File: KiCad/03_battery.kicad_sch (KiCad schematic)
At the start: 19 parts, among them IC301 MCP73831T-2ACI_OT, IC302 BQ29737DSER, J302 BM02B-GHS-TBT_LF__SN__N_, Q201 DMG3415U-7, Q202 T2N7002AK, Q500 T2N7002AK

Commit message: First scheme complete
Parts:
- renumbered C211 to C301, C212 to C302, C215 to C303, C214 to C304, C213 to C305, D202 to D301, D205 to D302, FB203 to FB301, J302 to J301, Q201 to Q301, Q202 to Q302, Q500 to Q303, R201 to R301, R206 to R302, R209 to R303, R210 to R304, R211 to R305

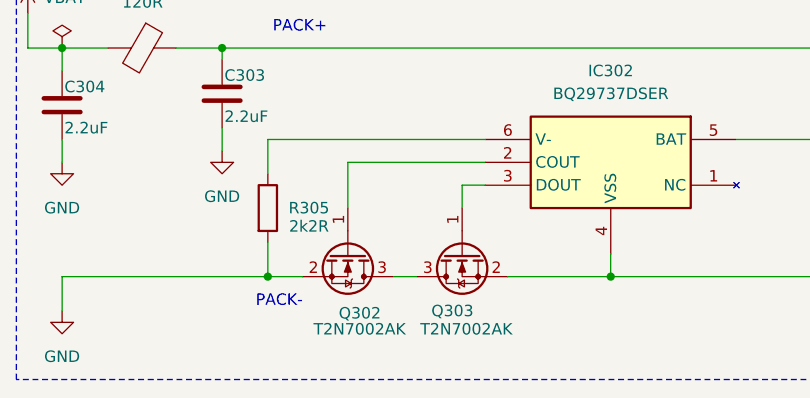
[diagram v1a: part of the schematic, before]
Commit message: ERC fixes
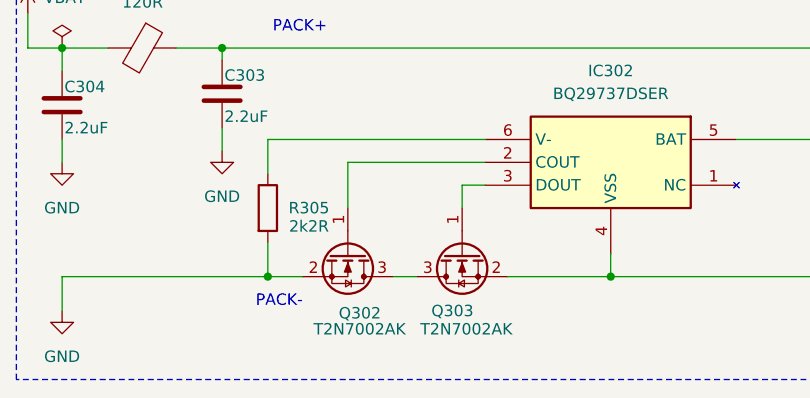
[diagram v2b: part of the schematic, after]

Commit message: minor pcb update
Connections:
- net COUT: now reaches IC302.2 (COUT), Q302.1 (G)
- net DOUT: now reaches IC302.3 (DOUT), Q303.1 (G)
- net V-: now reaches IC302.6 (V-), R305.1
- net BAT: now reaches C305.1, IC302.5 (BAT), R304.2

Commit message: Update FTDI pin header
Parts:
- R304: footprint Resistor_SMD:R_0805_2012Metric -> Resistor_SMD:R_0402_1005Metric
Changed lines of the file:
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@@
 			)
 		)
-		(property "Footprint" "Resistor_SMD:R_0805_2012Metric"
+		(property "Footprint" "Resistor_SMD:R_0402_1005Metric"
 			(at 135.382 143.51 90)
 			(effects

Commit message: Fill BOM table
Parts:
- IC301: Manufacturer (none) -> Microchip; Manufacturer Part Number (none) -> MCP73831T-2ACI/OT; Manufacturer_Name Microchip -> (none); Manufacturer_Part_Number MCP73831T-2ACI/OT -> (none); Mouser Part Number 579-MCP73831T-2ACIOT -> (none); Mouser Price/Stock https://www.mouser.co.uk/ProductDetail/Microchip-Technology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 -> (none)
- IC302: Manufacturer (none) -> Texas Instruments; Manufacturer Part Number (none) -> BQ29737DSER; Manufacturer_Name Texas Instruments -> (none); Manufacturer_Part_Number BQ29737DSER -> (none); Mouser Part Number 595-BQ29737DSER -> (none); Mouser Price/Stock https://www.mouser.co.uk/ProductDetail/Texas-Instruments/BQ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 -> (none)
- J301: Manufacturer (none) -> JST (JAPAN SOLDERLESS TERMINALS); Manufacturer Part Number (none) -> BM02B-GHS-TBT(LF)(SN)(N); Manufacturer_Name JST (JAPAN SOLDERLESS TERMINALS) -> (none); Manufacturer_Part_Number BM02B-GHS-TBT(LF)(SN)(N) -> (none)
- R303: LCSC link https://www.lcsc.com/product-detail/Chip-Resistor-Surface-M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 -> (none)
- R304: Manufacturer (none) -> UNI-ROYAL(Uniroyal Elec); Manufacturer Part Number (none) -> 0402WGF3300TCE
- R305: footprint Resistor_SMD:R_0805_2012Metric -> Resistor_SMD:R_0402_1005Metric; Manufacturer (none) -> UNI-ROYAL(Uniroyal Elec); Manufacturer Part Number (none) -> 0402WGF2201TCE
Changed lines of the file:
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@@
-			)
-		)
-		(property "Manufacturer_Name" "JST (JAPAN SOLDERLESS TERMINALS)"
-			(at 648.59 146.05 0)
-			(effects
-				(font
-					(size 1.27 1.27)
-				)
-				(justify left top)
-				(hide yes)
-			)
-		)
-		(property "Manufacturer_Part_Number" "BM02B-GHS-TBT(LF)(SN)(N)"
-			(at 748.59 146.05 0)
-			(effects
-				(font
-					(size 1.27 1.27)
-				)
-				(justify left top)
-				(hide yes)
-			)
-		)
-		(property "Mouser Part Number" ""
-			(at 848.59 146.05 0)
-			(effects
-				(font
-					(size 1.27 1.27)
-				)
-				(justify left top)
-				(hide yes)
-			)
-		)
-		(property "Mouser Price/Stock" ""
-			(at 948.59 146.05 0)
-			(effects
-				(font
-					(size 1.27 1.27)
-				)
-				(justify left top)
-				(hide yes)
 			)
 		)
@@
 				)
 				(justify left top)
+				(hide yes)
+			)
+		)
+		(property "Manufacturer" "JST (JAPAN SOLDERLESS TERMINALS)"
+			(at 153.67 162.56 90)
+			(effects
+				(font
+					(size 1.27 1.27)
+				)
+				(hide yes)
+			)
+		)
+		(property "Manufacturer Part Number" "BM02B-GHS-TBT(LF)(SN)(N)"
+			(at 153.67 162.56 90)
+			(effects
+				(font
+					(size 1.27 1.27)
+				)
 				(hide yes)
 			)
@@
 			)
 		)
-		(property "LCSC link" "https://www.lcsc.com/product-detail/Chip-Resistor-Surface-Mount_UNI-ROYAL-Uniroyal-Elec-0402WGF5101TCE_C25905.html"
-			(at 143.51 104.14 0)
-			(effects
-				(font
-					(size 1.27 1.27)
-				)
-				(hide yes)
-			)
-		)
 		(property "Manufacturer" "UNI-ROYAL(Uniroyal Elec)"
 			(at 143.51 104.14 0)
@@
 			)
 		)
-		(property "MANUFACTURER" ""
-			(at 100.33 87.63 0)
-			(effects
-				(font
-					(size 1.27 1.27)
-				)
-				(hide yes)
-			)
-		)
 		(property "PARTREV" ""
 			(at 100.33 87.63 0)
@@
 			)
 		)
-		(property "MANUFACTURER" ""
-			(at 48.26 144.78 0)
-			(effects
-				(font
-					(size 1.27 1.27)
-				)
-				(hide yes)
-			)
-		)
 		(property "PARTREV" ""
 			(at 48.26 144.78 0)
@@
 			)
 		)
-		(property "MANUFACTURER" ""
-			(at 66.04 143.51 0)
-			(effects
-				(font
-					(size 1.27 1.27)
-				)
-				(hide yes)
-			)
-		)
 		(property "PARTREV" ""
 			(at 66.04 143.51 0)
@@
 			)
 		)
-		(property "Footprint" "Resistor_SMD:R_0805_2012Metric"
+		(property "Footprint" "Resistor_SMD:R_0402_1005Metric"
 			(at 69.342 156.21 90)
 			(effects
@@
 			)
 		)
-		(property "Manufacturer" ""
+		(property "Manufacturer" "UNI-ROYAL(Uniroyal Elec)"
 			(at 71.12 156.21 0)
 			(effects
@@
 			)
 		)
-		(property "Manufacturer Part Number" ""
-			(at 71.12 156.21 0)
-			(effects
-				(font
-					(size 1.27 1.27)
-				)
-				(hide yes)
-			)
-		)
-		(property "MANUFACTURER" ""
+		(property "Manufacturer Part Number" "0402WGF2201TCE"
 			(at 71.12 156.21 0)
 			(effects
@@
 			)
 		)
-		(property "Manufacturer_Name" "Microchip"
-			(at 134.62 591.44 0)
-			(effects
-				(font
-					(size 1.27 1.27)
-				)
-				(justify left top)
-				(hide yes)
-			)
-		)
-		(property "Manufacturer_Part_Number" "MCP73831T-2ACI/OT"
-			(at 134.62 691.44 0)
-			(effects
-				(font
-					(size 1.27 1.27)
-				)
-				(justify left top)
-				(hide yes)
-			)
-		)
-		(property "Mouser Part Number" "579-MCP73831T-2ACIOT"
-			(at 134.62 791.44 0)
-			(effects
-				(font
-					(size 1.27 1.27)
-				)
-				(justify left top)
-				(hide yes)
-			)
-		)
-		(property "Mouser Price/Stock" "https://www.mouser.co.uk/ProductDetail/Microchip-Technology/MCP73831T-2ACI-OT?qs=yUQqVecv4qvbBQBGbHx0Mw%3D%3D"
-			(at 134.62 891.44 0)
-			(effects
-				(font
-					(size 1.27 1.27)
-				)
-				(justify left top)
-				(hide yes)
-			)
-		)
 		(property "Arrow Part Number" "MCP73831T-2ACI/OT"
 			(at 134.62 991.44 0)
@@
 				)
 				(justify left top)
+				(hide yes)
+			)
+		)
+		(property "Manufacturer" "Microchip"
+			(at 110.49 96.52 0)
+			(effects
+				(font
+					(size 1.27 1.27)
+				)
+				(hide yes)
+			)
+		)
+		(property "Manufacturer Part Number" "MCP73831T-2ACI/OT"
+			(at 110.49 96.52 0)
+			(effects
+				(font
+					(size 1.27 1.27)
+				)
 				(hide yes)
 			)
@@
 			)
 		)
-		(property "Manufacturer" ""
+		(property "Manufacturer" "UNI-ROYAL(Uniroyal Elec)"
 			(at 137.16 143.51 0)
 			(effects
@@
 			)
 		)
-		(property "Manufacturer Part Number" ""
-			(at 137.16 143.51 0)
-			(effects
-				(font
-					(size 1.27 1.27)
-				)
-				(hide yes)
-			)
-		)
-		(property "MANUFACTURER" ""
+		(property "Manufacturer Part Number" "0402WGF3300TCE"
 			(at 137.16 143.51 0)
 			(effects
@@
 			)
 		)
-		(property "MANUFACTURER" ""
-			(at 149.86 92.71 0)
-			(effects
-				(font
-					(size 1.27 1.27)
-				)
-				(hide yes)
-			)
-		)
 		(property "PARTREV" ""
 			(at 149.86 92.71 0)
@@
 			)
 		)
-		(property "Manufacturer_Name" "Texas Instruments"
-			(at 93.98 640.97 0)
-			(effects
-				(font
-					(size 1.27 1.27)
-				)
-				(justify left top)
-				(hide yes)
-			)
-		)
-		(property "Manufacturer_Part_Number" "BQ29737DSER"
-			(at 93.98 740.97 0)
-			(effects
-				(font
-					(size 1.27 1.27)
-				)
-				(justify left top)
-				(hide yes)
-			)
-		)
-		(property "Mouser Part Number" "595-BQ29737DSER"
-			(at 93.98 840.97 0)
-			(effects
-				(font
-					(size 1.27 1.27)
-				)
-				(justify left top)
-				(hide yes)
-			)
-		)
-		(property "Mouser Price/Stock" "https://www.mouser.co.uk/ProductDetail/Texas-Instruments/BQ29737DSER?qs=QNEnbhJQKvZFYvtkppP%2FHQ%3D%3D"
-			(at 93.98 940.97 0)
-			(effects
-				(font
-					(size 1.27 1.27)
-				)
-				(justify left top)
-				(hide yes)
-			)
-		)
 		(property "Arrow Part Number" "BQ29737DSER"
 			(at 93.98 1040.97 0)
@@
 				)
 				(justify left top)
+				(hide yes)
+			)
+		)
+		(property "Manufacturer" "Texas Instruments"
+			(at 118.11 146.05 0)
+			(effects
+				(font
+					(size 1.27 1.27)
+				)
+				(hide yes)
+			)
+		)
+		(property "Manufacturer Part Number" "BQ29737DSER"
+			(at 118.11 146.05 0)
+			(effects
+				(font
+					(size 1.27 1.27)
+				)
 				(hide yes)
 			)
@@
 			)
 		)
-		(property "MANUFACTURER" ""
-			(at 137.16 158.75 0)
-			(effects
-				(font
-					(size 1.27 1.27)
-				)
-				(hide yes)
-			)
-		)
 		(property "PARTREV" ""
 			(at 137.16 158.75 0)
@@
 			(at 132.08 53.34 0)
 			(effects
-				(font
-					(size 1.27 1.27)
-				)
-				(hide yes)
-			)
-		)
-		(property "MANUFACTURER" ""
-			(at 132.08 53.34 0)
-			(effects

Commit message: battery connector update
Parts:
- removed J301: BM02B-GHS-TBT_LF__SN__N_, psu:BM02B-GHS-TBT_1, symbol psu:BM02B-GHS-TBT_LF__SN__N_
- added J301: Conn_01x02, Connector_PinHeader_2.54mm:PinHeader_1x02_P2.54mm_Vertical, symbol Connector_Generic:Conn_01x02
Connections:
- net CELL+: now also J301.1 (Pin_1)
- net CELL-: now also J301.2 (Pin_2)
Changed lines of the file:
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@@
 	(wire
 		(pts
-			(xy 153.67 138.43) (xy 153.67 142.24)
+			(xy 153.67 138.43) (xy 153.67 149.86)
 		)
 		(stroke
@@
 	(wire
 		(pts
-			(xy 153.67 163.83) (xy 153.67 162.56)
+			(xy 153.67 152.4) (xy 153.67 163.83)
 		)
 		(stroke
@@
 	)
 	(symbol
-		(lib_id "psu:BM02B-GHS-TBT_LF__SN__N_")
-		(at 153.67 162.56 90)
-		(unit 1)
-		(exclude_from_sim no)
-		(in_bom yes)
-		(on_board yes)
-		(dnp no)
-		(property "Reference" "J301"
-			(at 145.288 152.4 90)
-			(effects
-				(font
-					(size 1.27 1.27)
-				)
-				(justify right)
-			)
-		)
-		(property "Value" "BM02B-GHS-TBT_LF__SN__N_"
-			(at 158.496 137.414 0)
-			(effects
-				(font
-					(size 1.27 1.27)
-				)
-				(justify right)
-			)
-		)
-		(property "Footprint" "psu:BM02B-GHS-TBT_1"
-			(at 248.59 146.05 0)
-			(effects
-				(font
-					(size 1.27 1.27)
-				)
-				(justify left top)
-				(hide yes)
-			)
-		)
-		(property "Datasheet" "http://www.jst-mfg.com/product/pdf/eng/eGH.pdf"
-			(at 348.59 146.05 0)
-			(effects
-				(font
-					(size 1.27 1.27)
-				)
-				(justify left top)
-				(hide yes)
-			)
-		)
-		(property "Description" "CONN HEADER GH TOP 2POS 1.25MM"
-			(at 159.004 149.606 0)
-			(effects
-				(font
-					(size 1.27 1.27)
-				)
-				(hide yes)
-			)
-		)
-		(property "Height" ""
-			(at 548.59 146.05 0)
-			(effects
-				(font
-					(size 1.27 1.27)
-				)
-				(justify left top)
-				(hide yes)
-			)
-		)
-		(property "Arrow Part Number" "BM02B-GHS-TBT(LF)(SN)(N)"
-			(at 1048.59 146.05 0)
-			(effects
-				(font
-					(size 1.27 1.27)
-				)
-				(justify left top)
-				(hide yes)
-			)
-		)
-		(property "Arrow Price/Stock" "https://www.arrow.com/en/products/bm02b-ghs-tbt-lf-sn-n/jst-manufacturing?region=nac"
-			(at 1148.59 146.05 0)
-			(effects
-				(font
-					(size 1.27 1.27)
-				)
-				(justify left top)
-				(hide yes)
-			)
-		)
-		(property "Manufacturer" "JST (JAPAN SOLDERLESS TERMINALS)"
-			(at 153.67 162.56 90)
-			(effects
-				(font
-					(size 1.27 1.27)
-				)
-				(hide yes)
-			)
-		)
-		(property "Manufacturer Part Number" "BM02B-GHS-TBT(LF)(SN)(N)"
-			(at 153.67 162.56 90)
-			(effects
-				(font
-					(size 1.27 1.27)
-				)
-				(hide yes)
-			)
-		)
-		(pin "2"
-		)
-		(pin "1"
-		)
-		(instances
-			(project ""
-				(path "/daadd221-9750-45f3-8ee2-46422755319d/b34b4305-fc5f-4a45-8a4d-fa6c9d60dff6"
-					(reference "J301")
-					(unit 1)
-				)
-			)
-		)
-	)
-	(symbol
 		(lib_id "Transistor_FET:T2N7002AK")
 		(at 92.71 161.29 90)
@@
 					(unit 1)
 				)
+			)
+		)
+	)
+	(symbol
+		(lib_id "Connector_Generic:Conn_01x02")
+		(at 158.75 149.86 0)
+		(unit 1)
+		(exclude_from_sim no)
+		(in_bom yes)
+		(on_board yes)
+		(dnp no)
+		(property "Reference" "J301"
+			(at 156.21 146.304 0)
+			(effects
+				(font
+					(size 1.27 1.27)
+				)
+				(justify left)
+			)
+		)
+		(property "Value" "Conn_01x02"
+			(at 153.416 155.702 0)
+			(effects
+				(font
+					(size 1.27 1.27)
+				)
+				(justify left)
+			)
+		)
+		(property "Footprint" "Connector_PinHeader_2.54mm:PinHeader_1x02_P2.54mm_Vertical"
+			(at 158.75 149.86 0)
+			(effects
+				(font
+					(size 1.27 1.27)
+				)
+				(hide yes)
+			)
+		)
+		(property "Datasheet" "~"
+			(at 158.75 149.86 0)
+			(effects
+				(font
+					(size 1.27 1.27)
+				)
+				(hide yes)
+			)
+		)
+		(property "Description" "Generic connector, single row, 01x02, script generated (kicad-library-utils/schlib/autogen/connector/)"
+			(at 158.75 149.86 0)
+			(effects
+				(font
+					(size 1.27 1.27)
+				)
+				(hide yes)
+			)
+		)
+		(pin "1"
+		)
+		(pin "2"
+		)
+		(instances
+			(project ""
+				(path "/daadd221-9750-45f3-8ee2-46422755319d/b34b4305-fc5f-4a45-8a4d-fa6c9d60dff6"
+					(reference "J301")
+					(unit 1)
+				)

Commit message: BOM updates
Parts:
- R301, R302, R303, R304, R305: Manufacturer UNI-ROYAL(Uniroyal Elec) -> UNI-ROYAL
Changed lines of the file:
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@@
 			)
 		)
-		(property "Manufacturer" "UNI-ROYAL(Uniroyal Elec)"
+		(property "Manufacturer" "UNI-ROYAL"
 			(at 88.9 91.44 0)
 			(effects
@@
 			)
 		)
-		(property "Manufacturer" "UNI-ROYAL(Uniroyal Elec)"
+		(property "Manufacturer" "UNI-ROYAL"
 			(at 143.51 104.14 0)
 			(effects
@@
 			)
 		)
-		(property "Manufacturer" "UNI-ROYAL(Uniroyal Elec)"
+		(property "Manufacturer" "UNI-ROYAL"
 			(at 71.12 156.21 0)
 			(effects
@@
 			)
 		)
-		(property "Manufacturer" "UNI-ROYAL(Uniroyal Elec)"
+		(property "Manufacturer" "UNI-ROYAL"
 			(at 137.16 143.51 0)
 			(effects
@@
 			)
 		)
-		(property "Manufacturer" "UNI-ROYAL(Uniroyal Elec)"
+		(property "Manufacturer" "UNI-ROYAL"
 			(at 132.08 53.34 0)
 			(effects
